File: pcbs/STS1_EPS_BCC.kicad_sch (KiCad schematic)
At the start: 45 parts, among them Q1 SI7135DP-T1-GE3, U1 LTC4020EUHFPBF, U2 SI7272DP-T1-GE3, U3 SI7272DP-T1-GE3

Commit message: Worked on STS1_EPS_1 layout.
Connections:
- net BATT: no longer U1.20 (BAT)
- new net BATT_RAW: U1.20 (BAT)
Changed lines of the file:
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@@
     (effects (font (size 1.27 1.27)) (justify left))
   )
-  (hierarchical_label "BATT" (shape output) (at 146.05 82.55 0)
+  (hierarchical_label "BATT_RAW" (shape output) (at 146.05 82.55 0)
     (effects (font (size 1.27 1.27)) (justify left))
   )

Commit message: Worked on STS1_EPS_1 layout.
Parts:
- added TP1: TestPoint, Connector_Pin:Pin_D0.7mm_L6.5mm_W1.8mm_FlatFork, symbol Connector:TestPoint
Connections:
- net BGATE: now also TP1.1
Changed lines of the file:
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@@
   (junction (at 232.41 24.13) (diameter 0) (color 0 0 0 0)
   )
+  (junction (at 246.38 43.18) (diameter 0) (color 0 0 0 0)
+  )
   (junction (at 135.89 173.99) (diameter 0) (color 0 0 0 0)
   )
@@
     (stroke (width 0) (type default) (color 0 0 0 0))
   )
+  (wire (pts (xy 246.38 43.18) (xy 236.22 43.18))
+    (stroke (width 0) (type default) (color 0 0 0 0))
+  )
   (wire (pts (xy 232.41 69.85) (xy 232.41 72.39))
     (stroke (width 0) (type default) (color 0 0 0 0))
@@
     (stroke (width 0) (type default) (color 0 0 0 0))
   )
+  (wire (pts (xy 246.38 42.545) (xy 246.38 43.18))
+    (stroke (width 0) (type default) (color 0 0 0 0))
+  )
   (wire (pts (xy 52.07 100.33) (xy 52.07 102.87))
     (stroke (width 0) (type default) (color 0 0 0 0))
@@
     (stroke (width 0) (type default) (color 0 0 0 0))
   )
-  (wire (pts (xy 260.35 43.18) (xy 255.27 43.18))
+  (wire (pts (xy 246.38 43.18) (xy 260.35 43.18))
     (stroke (width 0) (type default) (color 0 0 0 0))
   )
@@
     (effects (font (size 1.27 1.27)) (justify left bottom))
   )
-  (label "BGATE" (at 255.27 43.18 0)
+  (label "BGATE" (at 236.22 43.18 0)
     (effects (font (size 1.27 1.27)) (justify left bottom))
   )
@@
     (pin "9")
   )
+  (symbol (lib_id "Connector:TestPoint") (at 246.38 42.545 0) (unit 1)
+    (in_bom yes) (on_board yes) (fields_autoplaced)
+    (property "Reference" "TP1" (id 0) (at 248.285 37.9729 0)
+      (effects (font (size 1.27 1.27)) (justify left))
+    )
+    (property "Value" "TestPoint" (id 1) (at 248.285 40.5129 0)
+      (effects (font (size 1.27 1.27)) (justify left))
+    )
+    (property "Footprint" "Connector_Pin:Pin_D0.7mm_L6.5mm_W1.8mm_FlatFork" (id 2) (at 251.46 42.545 0)
+      (effects (font (size 1.27 1.27)) hide)
+    )
+    (property "Datasheet" "~" (id 3) (at 251.46 42.545 0)
+      (effects (font (size 1.27 1.27)) hide)
+    )
+    (pin "1")
+  )
   (symbol (lib_id "power:GND") (at 74.93 59.69 270) (unit 1)

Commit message: Added testpoints to STS1_EPS_1.
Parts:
- added TP10, TP11, TP4, TP5, TP6, TP7, TP8, TP9: TestPoint, TestPoint:TestPoint_THTPad_D1.0mm_Drill0.5mm, symbol Connector:TestPoint
- TP1: footprint Connector_Pin:Pin_D0.7mm_L6.5mm_W1.8mm_FlatFork -> TestPoint:TestPoint_THTPad_D1.0mm_Drill0.5mm
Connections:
- net BATT: now also TP11.1
- net BG1: now also TP7.1
- net BG2: now also TP9.1
- net MPPT_BUS: now also TP4.1
- net SHDN: now also TP5.1
- net TG1: now also TP6.1
- net TG2: now also TP8.1
- net VOUT: now also TP10.1

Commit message: worked on sts1_eps_1
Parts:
- R3: value 180k -> 187k
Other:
- note added: "Sets 7,2V float voltage."
- note removed: "Sets 7V float voltage."
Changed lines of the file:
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@@
     (effects (font (size 1.27 1.27)) (justify left bottom))
   )
-  (text "Sets 7V float voltage." (at 15.24 46.99 0)
+  (text "Sets 7,2V float voltage." (at 15.24 46.99 0)
     (effects (font (size 1.27 1.27)) (justify left bottom))
   )
@@
       (effects (font (size 1.27 1.27)) (justify right))
     )
-    (property "Value" "180k" (id 1) (at 27.432 56.007 0)
-      (effects (font (size 1.27 1.27)) (justify right))
-    )
+    (property "Value" "187k" (id 1) (at 27.432 56.007 0)
+      (effects (font (size 1.27 1.27)) (justify right))
+    )

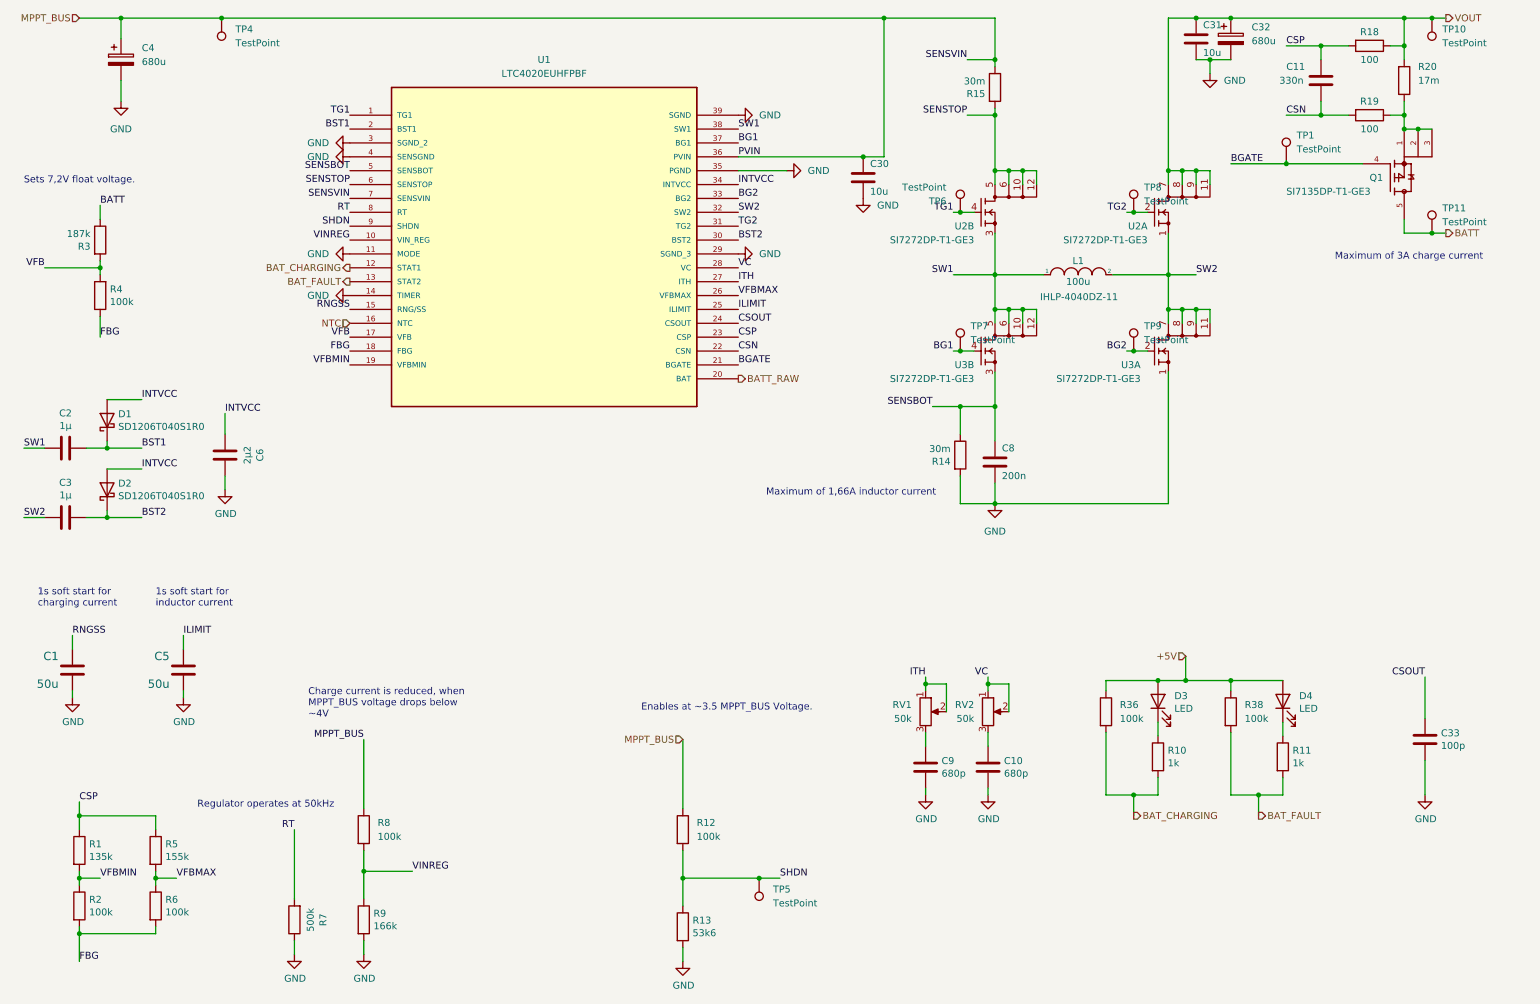
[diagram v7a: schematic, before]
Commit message: Worked on STS1_EPS_1.
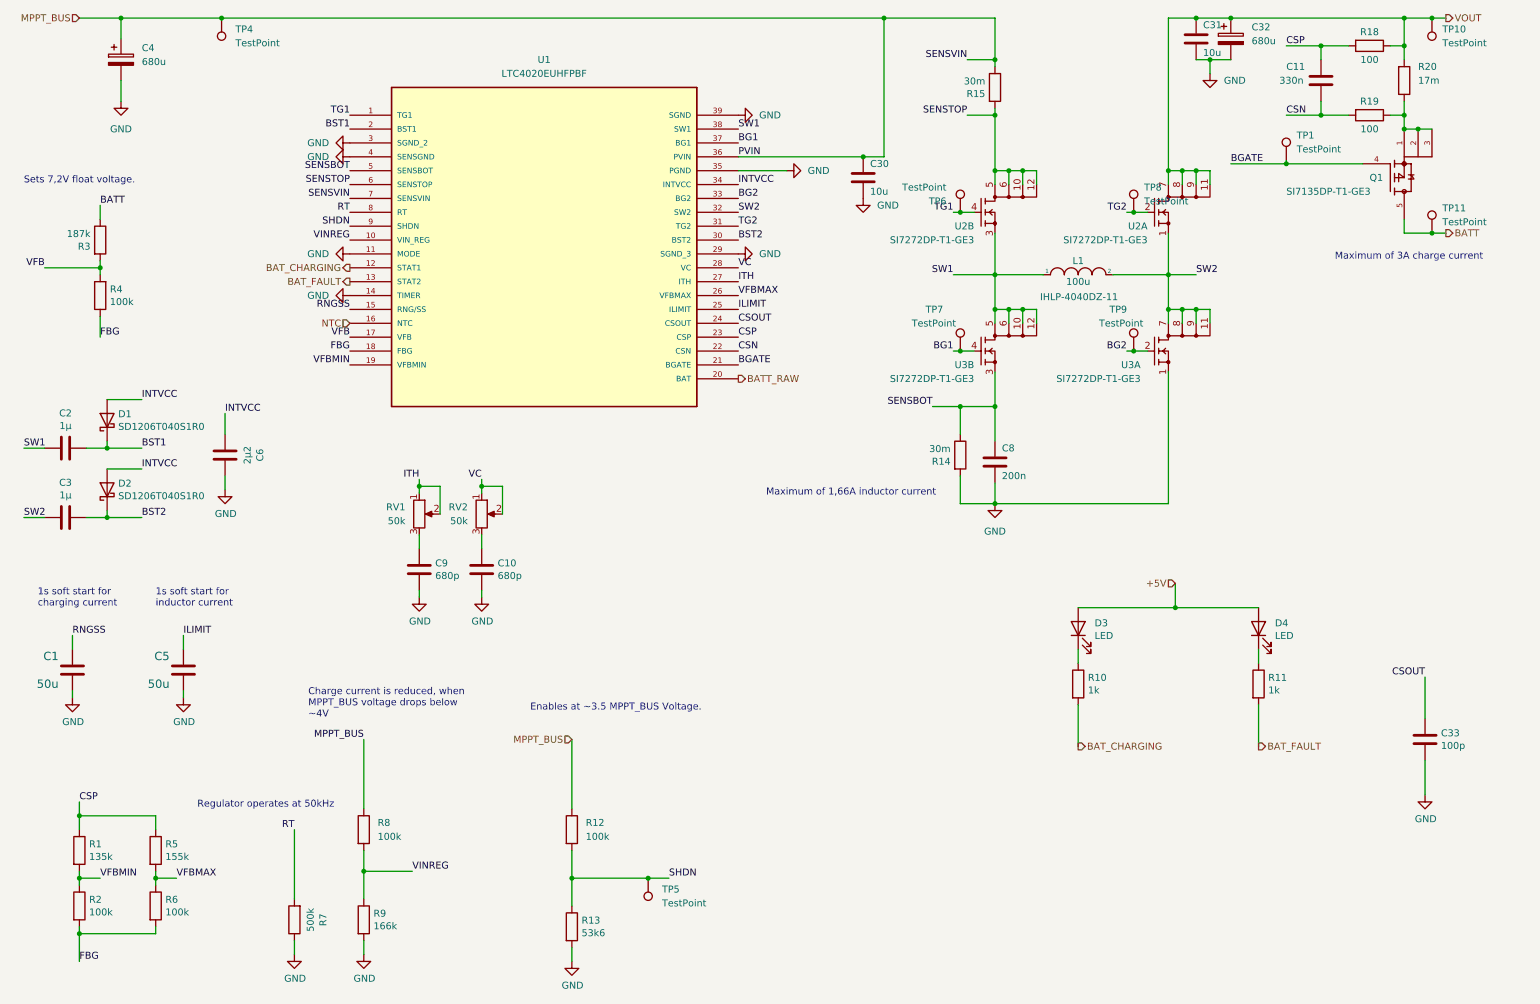
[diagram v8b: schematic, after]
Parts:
- removed R36, R38: 100k, Resistor_SMD:R_0805_2012Metric, symbol Device:R
- Q1: footprint STS_Package_SO:POWERPAK_SO8_single -> TRANS_SI7135DP-T1-GE3
- U1: footprint STS_Package_DFN_QFN:AD_QFN-38_UHF -> QFN-38_UHF
- U2, U3: footprint STS_Package_SO:POWERPAK_SO8 -> SI7288DPT1GE3
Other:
- moved on the sheet: C10, C9, D3, D4, R10, R11, R12, R13, RV1, RV2, TP5
